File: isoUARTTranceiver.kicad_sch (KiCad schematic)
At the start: 3 parts, among them J1 CONN HEADER VERT 2POS 1.5MM, U2 TLE9015DQUXUMA1

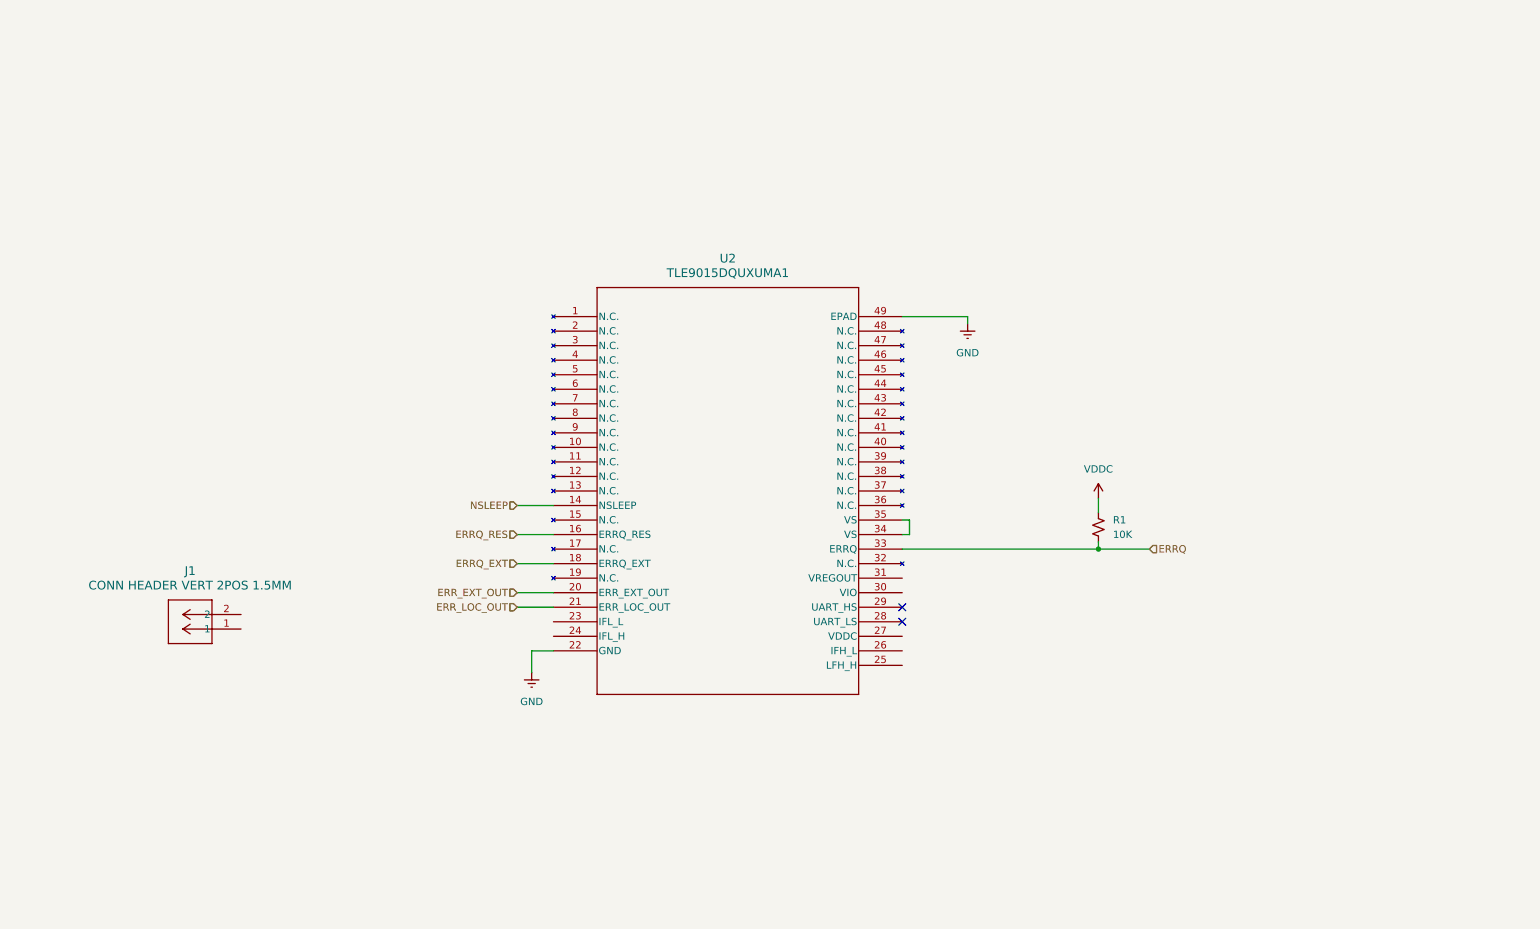
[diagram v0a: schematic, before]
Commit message: added stm pins
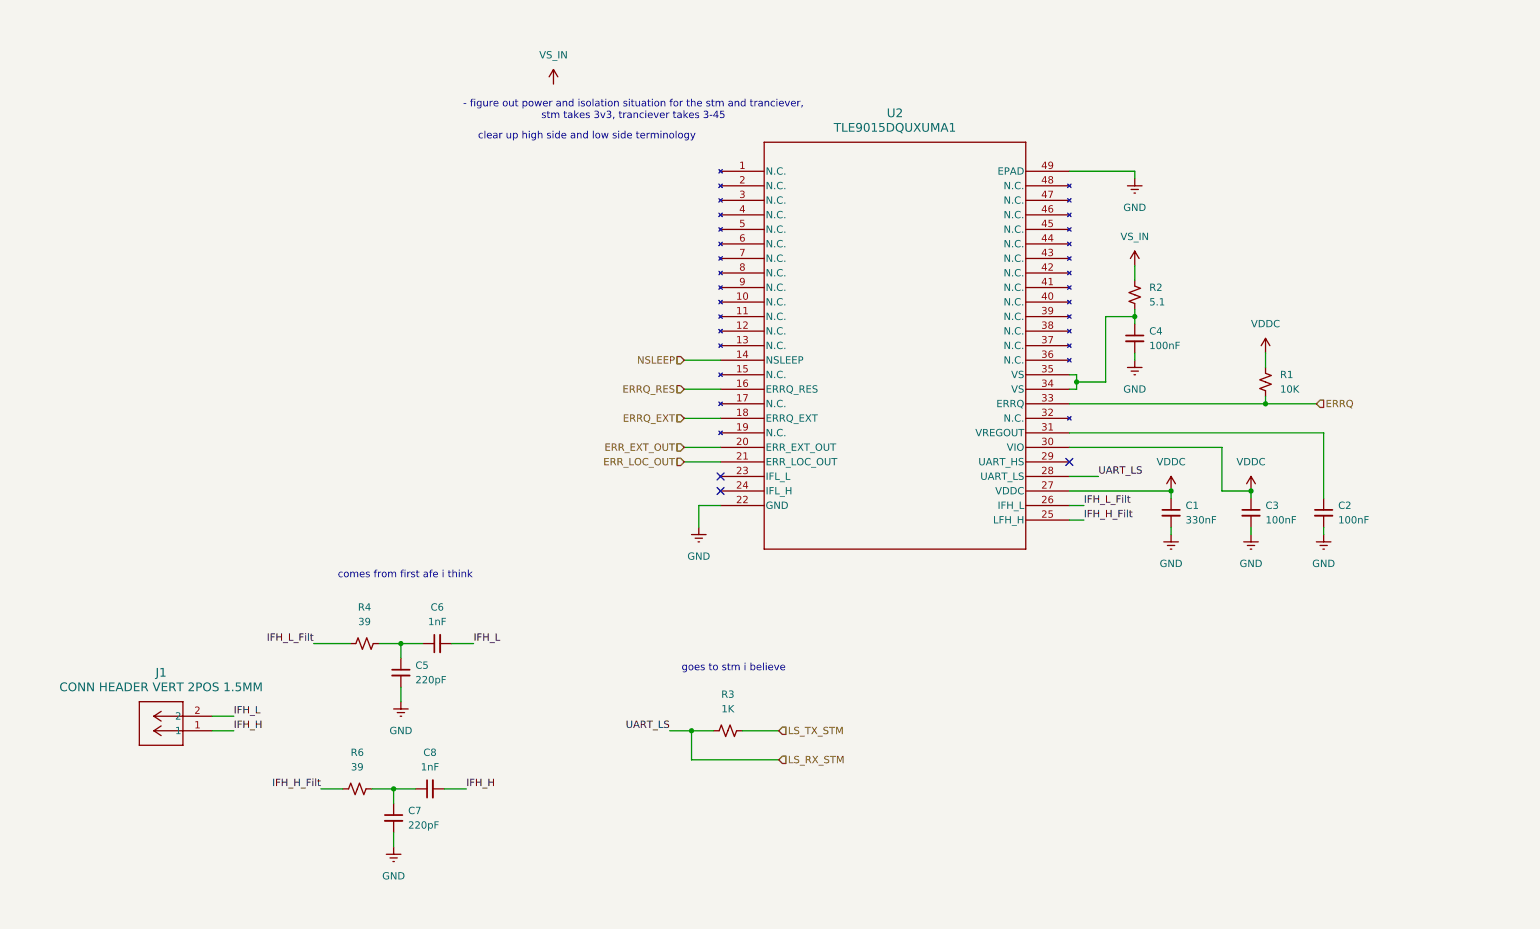
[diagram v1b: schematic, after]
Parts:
- added C1: 330nF, symbol Device:C_Small
- added C2, C3, C4: 100nF, symbol Device:C_Small
- added C5, C7: 220pF, symbol Device:C_Small
- added C6, C8: 1nF, symbol Device:C_Small
- added R2: 5.1, symbol Device:R_Small_US
- added R3: 1K, symbol Device:R_Small_US
- added R4, R6: 39, symbol Device:R_Small_US
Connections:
- net GND: now also C1.2, C2.2, C3.2, C4.2, C5.2, C7.2
- net VDDC: now also U2.27 (VDDC), U2.30 (VIO), C1.1, C3.1
- net IFH_H_Filt: now reaches U2.25 (LFH_H)
- net IFH_H_Filt: now also R6.1
- net IFH_L_Filt: now reaches U2.26 (IFH_L)
- net IFH_L_Filt: now also R4.1
- net LS_RX_STM: now reaches U2.28 (UART_LS)
- net LS_RX_STM: now also R3.1
- net at U2.31 (VREGOUT): now also C2.1
- net at U2.34 (VS), U2.35 (VS): now also C4.1, R2.2
- net IFH_H: now reaches J1.1
- net IFH_H: now also C8.2
- net IFH_L: now reaches J1.2
- net IFH_L: now also C6.2
- new net: C7.1, C8.1, R6.2
- new net: C5.1, C6.1, R4.2
- new net LS_TX_STM: R3.2
- new net VS_IN: R2.1
- no-connect marks 2 -> 3
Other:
- note added: "- figure out power and isolation situation for the stm and tranciever, stm takes 3v3, tranciever takes 3-45"
- note added: "clear up high side and low side terminology"
- note added: "comes from first afe i think"
- note added: "goes to stm i believe"
- moved on the sheet: J1, R1, U2

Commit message: finished can and power
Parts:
- removed J1: CONN HEADER VERT 2POS 1.5MM, footprints:CONN_B2B-ZR_02P_JST, symbol symbols:B2B-ZR
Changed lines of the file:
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@@
-	(wire
-		(pts
-			(xy 52.07 143.51) (xy 55.88 143.51)
-		)
-		(stroke
-			(width 0)
-			(type default)
-		)
-	)
 	(wire
 		(pts
@@
 		(pts
 			(xy 246.38 110.49) (xy 246.38 111.76)
-		)
-		(stroke
-			(width 0)
-			(type default)
-		)
-	)
-	(wire
-		(pts
-			(xy 52.07 146.05) (xy 55.88 146.05)
 		)
 		(stroke
@@
 		)
 	)
-	(label "IFH_H"
-		(at 55.88 146.05 0)
-		(effects
-			(font
-				(size 1.27 1.27)
-			)
-			(justify left bottom)
-		)
-	)
 	(label "IFH_L_Filt"
 		(at 204.47 106.68 0)
@@
 		)
 	)
-	(label "IFH_L"
-		(at 97.79 130.81 0)
-		(effects
-			(font
-				(size 1.27 1.27)
-			)
-			(justify left bottom)
-		)
-	)
 	(label "IFH_H_Filt"
 		(at 204.47 109.22 0)
@@
 		)
 	)
-	(label "IFH_L"
-		(at 55.88 143.51 0)
-		(effects
-			(font
-				(size 1.27 1.27)
-			)
-			(justify left bottom)
-		)
-	)
 	(label "IFH_H_Filt"
 		(at 71.12 156.21 180)
@@
 	(label "UART_LS"
 		(at 207.01 101.6 0)
-		(effects
-			(font
-				(size 1.27 1.27)
-			)
-			(justify left bottom)
-		)
-	)
-	(label "IFH_H"
-		(at 96.52 156.21 0)
 		(effects
 			(font
@@
 		)
 	)
+	(hierarchical_label "IFH_H"
+		(shape input)
+		(at 96.52 156.21 0)
+		(effects
+			(font
+				(size 1.27 1.27)
+			)
+			(justify left)
+		)
+	)
 	(hierarchical_label "ERRQ_EXT"
 		(shape input)
@@
 			)
 			(justify right)
+		)
+	)
+	(hierarchical_label "IFH_L"
+		(shape input)
+		(at 97.79 130.81 0)
+		(effects
+			(font
+				(size 1.27 1.27)
+			)
+			(justify left)
 		)
 	)
@@
 					(unit 1)
 				)
-			)
-		)
-	)
-	(symbol
-		(lib_id "symbols:B2B-ZR")
-		(at 52.07 146.05 180)
-		(unit 1)
-		(body_style 1)
-		(exclude_from_sim no)
-		(in_bom yes)
-		(on_board yes)
-		(in_pos_files yes)
-		(dnp no)
-		(fields_autoplaced yes)
-		(property "Reference" "J1"
-			(at 43.18 135.89 0)
-			(show_name no)
-			(do_not_autoplace no)
-			(effects
-				(font
-					(size 1.524 1.524)
-				)
-			)
-		)
-		(property "Value" "CONN HEADER VERT 2POS 1.5MM"
-			(at 43.18 138.43 0)
-			(show_name no)
-			(do_not_autoplace no)
-			(effects
-				(font
-					(size 1.524 1.524)
-				)
-			)
-		)
-		(property "Footprint" "footprints:CONN_B2B-ZR_02P_JST"
-			(at 52.07 146.05 0)
-			(hide yes)
-			(show_name no)
-			(do_not_autoplace no)
-			(effects
-				(font
-					(size 1.27 1.27)
-					(italic yes)
-				)
-			)
-		)
-		(property "Datasheet" "https://www.digikey.ca/en/products/detail/jst-sales-america-inc/B2B-ZR/926564"
-			(at 52.07 146.05 0)
-			(hide yes)
-			(show_name no)
-			(do_not_autoplace no)
-			(effects
-				(font
-					(size 1.27 1.27)
-					(italic yes)
-				)
-			)
-		)
-		(property "Description" "Connector Header Through Hole 2 position 0.059\" (1.50mm)"
-			(at 52.07 146.05 0)
-			(hide yes)
-			(show_name no)
-			(do_not_autoplace no)
-			(effects
-				(font
-					(size 1.27 1.27)
-				)
-			)
-		)
-		(pin "1"
-		)
-		(pin "2"
-		)
-		(instances
-			(project "bms-main"
-				(path "/d7e1c873-142c-4805-8303-47f5b9830fe8/4e7a0d49-6a60-4c8b-a4ed-2f153f3389c3"
-					(reference "J1")
-					(unit 1)
-				)

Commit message: schematic done
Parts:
- added R15: 0, symbol Device:R_Small_US
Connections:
- net LS_RX_STM: now also R15.2; no longer R3.1, U2.28 (UART_LS)
- net VS_IN renamed 5V
- new net UART_LS: R15.1, R3.1, U2.28 (UART_LS)
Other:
- moved on the sheet: R3
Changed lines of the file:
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@@
 	(text "goes to stm i believe"
 		(exclude_from_sim no)
-		(at 143.256 135.128 0)
+		(at 145.034 131.572 0)
 		(effects
 			(font
@@
 	)
 	(junction
-		(at 135.89 146.05)
+		(at 137.16 142.24)
 		(diameter 0)
 		(color 0 0 0 0)
@@
 	(wire
 		(pts
-			(xy 135.89 146.05) (xy 139.7 146.05)
+			(xy 137.16 142.24) (xy 140.97 142.24)
 		)
 		(stroke
@@
 	(wire
 		(pts
+			(xy 137.16 151.13) (xy 140.97 151.13)
+		)
+		(stroke
+			(width 0)
+			(type default)
+		)
+	)
+	(wire
+		(pts
 			(xy 81.28 130.81) (xy 85.09 130.81)
 		)
@@
 	(wire
 		(pts
-			(xy 144.78 146.05) (xy 151.13 146.05)
+			(xy 146.05 142.24) (xy 152.4 142.24)
 		)
 		(stroke
@@
 	(wire
 		(pts
-			(xy 132.08 146.05) (xy 135.89 146.05)
+			(xy 133.35 142.24) (xy 137.16 142.24)
 		)
 		(stroke
@@
 	(wire
 		(pts
-			(xy 135.89 151.13) (xy 135.89 146.05)
+			(xy 137.16 142.24) (xy 137.16 151.13)
 		)
 		(stroke
@@
 	(wire
 		(pts
-			(xy 151.13 151.13) (xy 135.89 151.13)
+			(xy 152.4 151.13) (xy 146.05 151.13)
 		)
 		(stroke
@@
 	)
 	(label "UART_LS"
-		(at 132.08 146.05 180)
+		(at 133.35 142.24 180)
 		(effects
 			(font
@@
 	(hierarchical_label "LS_TX_STM"
 		(shape input)
-		(at 151.13 146.05 0)
+		(at 152.4 142.24 0)
 		(effects
 			(font
@@
 	(hierarchical_label "LS_RX_STM"
 		(shape input)
-		(at 151.13 151.13 0)
+		(at 152.4 151.13 0)
 		(effects
 			(font
@@
 	)
 	(symbol
-		(lib_id "power:VDDA")
-		(at 111.76 33.02 0)
-		(unit 1)
-		(body_style 1)
-		(exclude_from_sim no)
-		(in_bom yes)
-		(on_board yes)
-		(in_pos_files yes)
-		(dnp no)
-		(fields_autoplaced yes)
-		(property "Reference" "#PWR012"
-			(at 111.76 36.83 0)
-			(hide yes)
-			(show_name no)
-			(do_not_autoplace no)
-			(effects
-				(font
-					(size 1.27 1.27)
-				)
-			)
-		)
-		(property "Value" "VS_IN"
-			(at 111.76 27.94 0)
-			(show_name no)
-			(do_not_autoplace no)
-			(effects
-				(font
-					(size 1.27 1.27)
-				)
-			)
-		)
-		(property "Footprint" ""
-			(at 111.76 33.02 0)
-			(hide yes)
-			(show_name no)
-			(do_not_autoplace no)
-			(effects
-				(font
-					(size 1.27 1.27)
-				)
-			)
-		)
-		(property "Datasheet" ""
-			(at 111.76 33.02 0)
-			(hide yes)
-			(show_name no)
-			(do_not_autoplace no)
-			(effects
-				(font
-					(size 1.27 1.27)
-				)
-			)
-		)
-		(property "Description" "Power symbol creates a global label with name \"VDDA\""
-			(at 111.76 33.02 0)
-			(hide yes)
-			(show_name no)
-			(do_not_autoplace no)
-			(effects
-				(font
-					(size 1.27 1.27)
-				)
-			)
-		)
-		(pin "1"
-		)
-		(instances
-			(project "bms-main"
-				(path "/d7e1c873-142c-4805-8303-47f5b9830fe8/4e7a0d49-6a60-4c8b-a4ed-2f153f3389c3"
-					(reference "#PWR012")
-					(unit 1)
-				)
-			)
-		)
-	)
-	(symbol
 		(lib_id "Device:C_Small")
 		(at 83.82 161.29 0)
@@
 			)
 		)
-		(property "Value" "VS_IN"
-			(at 213.36 59.69 0)
-			(show_name no)
-			(do_not_autoplace no)
-			(effects
-				(font
-					(size 1.27 1.27)
-				)
+		(property "Value" "5V"
+			(at 215.9 63.4999 0)
+			(show_name no)
+			(do_not_autoplace no)
+			(effects
+				(font
+					(size 1.27 1.27)
+				)
+				(justify left)
 			)
 		)
@@
 	(symbol
 		(lib_id "Device:R_Small_US")
-		(at 142.24 146.05 90)
+		(at 143.51 151.13 90)
+		(unit 1)
+		(body_style 1)
+		(exclude_from_sim no)
+		(in_bom yes)
+		(on_board yes)
+		(in_pos_files yes)
+		(dnp no)
+		(property "Reference" "R15"
+			(at 144.018 146.05 90)
+			(show_name no)
+			(do_not_autoplace no)
+			(effects
+				(font
+					(size 1.27 1.27)
+				)
+			)
+		)
+		(property "Value" "0"
+			(at 143.51 148.082 90)
+			(show_name no)
+			(do_not_autoplace no)
+			(effects
+				(font
+					(size 1.27 1.27)
+				)
+			)
+		)
+		(property "Footprint" ""
+			(at 143.51 151.13 0)
+			(hide yes)
+			(show_name no)
+			(do_not_autoplace no)
+			(effects
+				(font
+					(size 1.27 1.27)
+				)
+			)
+		)
+		(property "Datasheet" ""
+			(at 143.51 151.13 0)
+			(hide yes)
+			(show_name no)
+			(do_not_autoplace no)
+			(effects
+				(font
+					(size 1.27 1.27)
+				)
+			)
+		)
+		(property "Description" "Resistor, small US symbol"
+			(at 143.51 151.13 0)
+			(hide yes)
+			(show_name no)
+			(do_not_autoplace no)
+			(effects
+				(font
+					(size 1.27 1.27)
+				)
+			)
+		)
+		(pin "2"
+		)
+		(pin "1"
+		)
+		(instances
+			(project "bms-main"
+				(path "/d7e1c873-142c-4805-8303-47f5b9830fe8/4e7a0d49-6a60-4c8b-a4ed-2f153f3389c3"
+					(reference "R15")
+					(unit 1)
+				)
+			)
+		)
+	)
+	(symbol
+		(lib_id "Device:R_Small_US")
+		(at 143.51 142.24 90)
 		(unit 1)
 		(body_style 1)
@@
 		(fields_autoplaced yes)
 		(property "Reference" "R3"
-			(at 142.24 139.7 90)
+			(at 143.51 135.89 90)
 			(show_name no)
 			(do_not_autoplace no)
@@
 		)
 		(property "Value" "1K"
-			(at 142.24 142.24 90)
+			(at 143.51 138.43 90)
 			(show_name no)
 			(do_not_autoplace no)
@@
 		)
 		(property "Footprint" ""
-			(at 142.24 146.05 0)
+			(at 143.51 142.24 0)
 			(hide yes)
 			(show_name no)
@@
 		)
 		(property "Datasheet" ""
-			(at 142.24 146.05 0)
+			(at 143.51 142.24 0)
 			(hide yes)
 			(show_name no)
@@
 		)
 		(property "Description" "Resistor, small US symbol"
-			(at 142.24 146.05 0)
-			(hide yes)
-			(show_name no)
+			(at 143.51 142.24 0)
+			(hide yes)
+			(show_name no)

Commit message: fixed schematic a little
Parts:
- added R16, R17, R19, R20: 10K, symbol Device:R_Small_US
- added R18: 1K, symbol Device:R_Small_US
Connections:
- net VDDC is gone; now on net 5V: C1.1, C3.1, R1.1, U2.27 (VDDC), U2.30 (VIO)
- net 5V: now also R16.1, R17.1, R19.1, R20.1
- net ERRQ_EXT: now also R20.2
- net ERRQ_RES: now also R17.2
- net ERR_EXT_OUT: now also R19.2
- net GND: now also U2.1 (N.C.), U2.10 (N.C.), U2.11 (N.C.), U2.12 (N.C.), U2.13 (N.C.), U2.15 (N.C.), U2.17 (N.C.), U2.19 (N.C.), U2.2 (N.C.), U2.3 (N.C.), U2.32 (N.C.), U2.36 (N.C.), U2.37 (N.C.), U2.38 (N.C.), U2.39 (N.C.), U2.4 (N.C.), U2.40 (N.C.), U2.41 (N.C.), U2.42 (N.C.), U2.43 (N.C.), U2.44 (N.C.), U2.45 (N.C.), U2.46 (N.C.), U2.47 (N.C.), U2.48 (N.C.), U2.5 (N.C.), U2.6 (N.C.), U2.7 (N.C.), U2.8 (N.C.), U2.9 (N.C.)
- net IFH_H: now also R18.1
- net IFH_L: now also R18.2
- net NSLEEP: now also R16.2
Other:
- note added: "add damping resistor for other side of transceiver IC too, see datasheet, on afe"
- note added: "damping resistor"

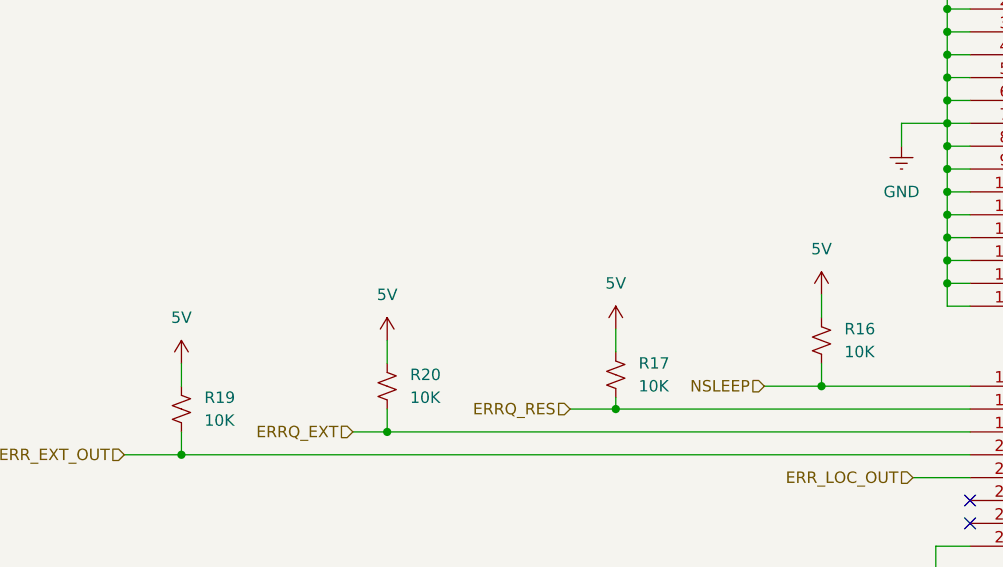
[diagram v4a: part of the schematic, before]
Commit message: fixed csense connectors and stm
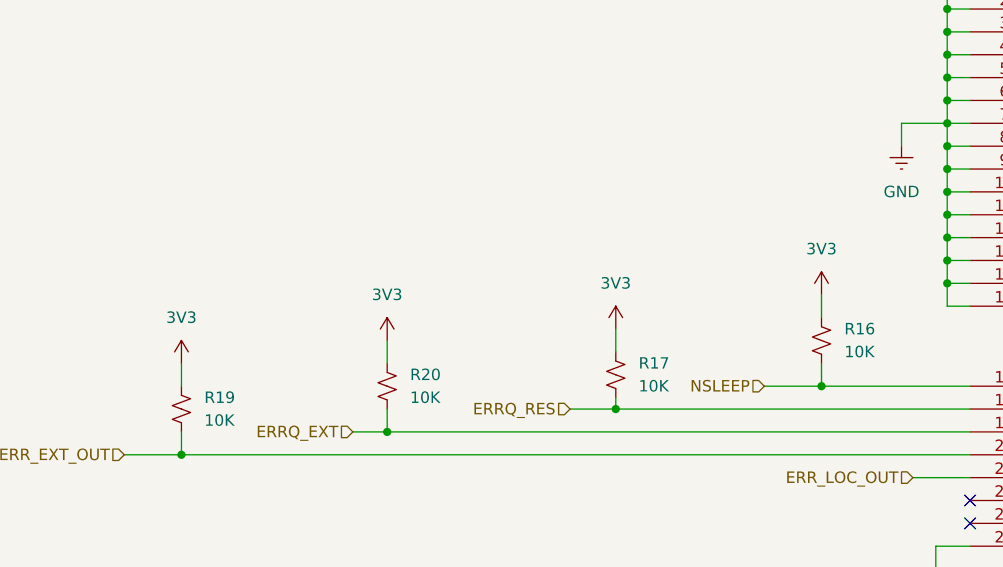
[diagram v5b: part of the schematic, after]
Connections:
- net 5V: no longer R16.1, R17.1, R19.1, R20.1
- new net 3V3: R16.1, R17.1, R19.1, R20.1
